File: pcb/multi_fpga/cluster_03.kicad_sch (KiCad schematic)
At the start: 7 parts, among them J15 Cluster3_SpokeBus, J16 Cluster3_Power

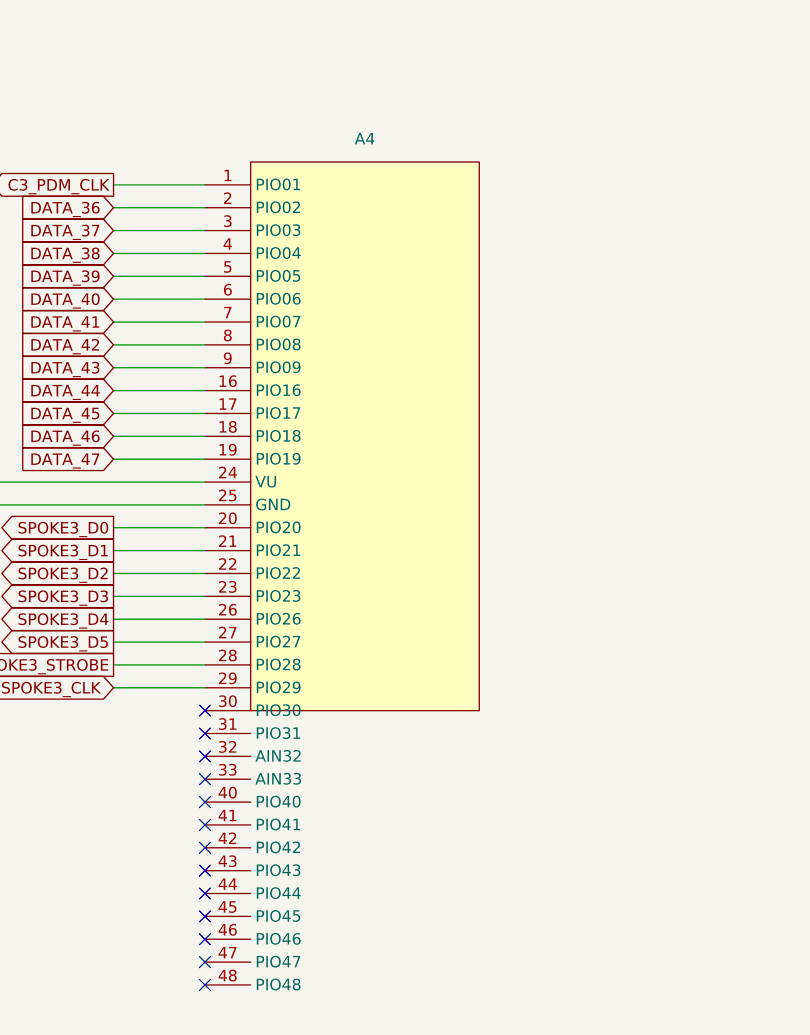
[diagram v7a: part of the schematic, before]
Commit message: Updated FPGA symbols.
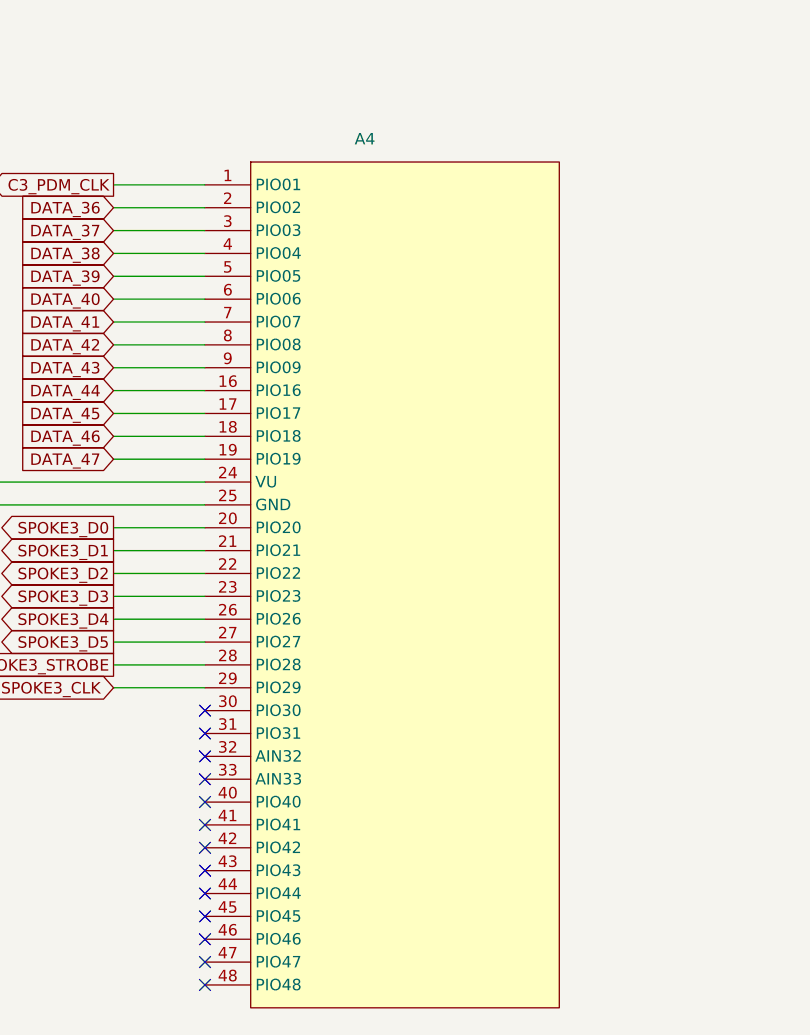
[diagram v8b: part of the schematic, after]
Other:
- moved on the sheet: A4
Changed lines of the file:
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@@
 		(color 0 0 0 0)
 	)
+	(no_connect
+		(at 205.74 196.85)
+	)
+	(no_connect
+		(at 205.74 199.39)
+	)
+	(no_connect
+		(at 205.74 189.23)
+	)
+	(no_connect
+		(at 205.74 204.47)
+	)
+	(no_connect
+		(at 205.74 181.61)
+	)
+	(no_connect
+		(at 205.74 176.53)
+	)
+	(no_connect
+		(at 205.74 186.69)
+	)
+	(no_connect
+		(at 205.74 179.07)
+	)
+	(no_connect
+		(at 205.74 191.77)
+	)
+	(no_connect
+		(at 205.74 173.99)
+	)
+	(no_connect
+		(at 205.74 194.31)
+	)
+	(no_connect
+		(at 205.74 201.93)
+	)
+	(no_connect
+		(at 205.74 184.15)
+	)
 	(wire
 		(pts
@@
 			)
 		)
-		(property "Description" ""
+		(property "Description" "100 nF decoupling capacitor, 0402"
 			(at 327.66 186.69 0)
 			(hide yes)
@@
 			)
 		)
-		(property "Description" ""
+		(property "Description" "Power symbol creates a global label with name \"GND\" , ground"
 			(at 308.61 191.77 0)
 			(hide yes)
@@
 	)
 	(symbol
-		(lib_name "GND_9")
 		(lib_id "power:GND")
 		(at 364.49 113.03 0)
@@
 	)
 	(symbol
-		(lib_name "GND_1")
 		(lib_id "power:GND")
 		(at 160.02 160.02 0)
@@
 			)
 		)
-		(property "Description" ""
+		(property "Description" "Power symbol creates a global label with name \"GND\" , ground"
 			(at 175.26 154.94 0)
 			(hide yes)
@@
 			)
 		)
-		(property "Description" ""
+		(property "Description" "100 nF decoupling capacitor, 0402"
 			(at 289.56 186.69 0)
 			(hide yes)
@@
 			)
 		)
-		(property "Datasheet" ""
+		(property "Datasheet" "http://ww1.microchip.com/downloads/en/DeviceDoc/20001826D.pdf"
 			(at 308.61 181.61 0)
 			(hide yes)
@@
 			)
 		)
-		(property "Description" ""
+		(property "Description" "250mA Low Quiscent Current LDO, 1.8V output, SOT-23"
 			(at 308.61 181.61 0)
 			(hide yes)
@@
 			)
 		)
-		(property "Description" ""
+		(property "Description" "Cluster FPGA module — Pmod JA (8 sig, 200ohm series) + DIP header (13 of 32 GPIO used for local PDM capture); every pin series-resistor protected, no differential-capable I/O (see PHASE4.md Spoke link)"
 			(at 223.52 143.51 0)
 			(hide yes)
@@
 			)
 		)
-		(pin "D1"
+		(pin "1"
+		)
+		(pin "2"
+		)
+		(pin "3"
+		)
+		(pin "4"
+		)
+		(pin "5"
+		)
+		(pin "6"
+		)
+		(pin "7"
+		)
+		(pin "8"
+		)
+		(pin "9"
+		)
+		(pin "16"
+		)
+		(pin "17"
 		)
-		(pin "D2"
+		(pin "18"
 		)
-		(pin "D3"
+		(pin "19"
 		)
-		(pin "D4"
+		(pin "20"
 		)
-		(pin "D5"
+		(pin "21"
 		)
-		(pin "D6"
+		(pin "22"
 		)
-		(pin "D7"
+		(pin "23"
 		)
-		(pin "D8"
+		(pin "24"
 		)
-		(pin "D9"
+		(pin "25"
 		)
-		(pin "D10"
+		(pin "26"
 		)
-		(pin "D11"
+		(pin "27"
 		)
-		(pin "D12"
+		(pin "28"
 		)
-		(pin "D13"
+		(pin "29"
 		)
-		(pin "D24"
+		(pin "30"
 		)
-		(pin "D25"
+		(pin "31"
 		)
-		(pin "D16"
+		(pin "32"
 		)
-		(pin "D17"
+		(pin "33"
 		)
-		(pin "D18"
+		(pin "40"
 		)
-		(pin "D19"
+		(pin "41"
 		)
-		(pin "D20"
+		(pin "42"
 		)
-		(pin "D21"
+		(pin "43"
 		)
-		(pin "D22"
+		(pin "44"
 		)
-		(pin "D23"
+		(pin "45"
+		)
+		(pin "46"
+		)
+		(pin "47"
+		)
+		(pin "48"
 		)
 		(instances
@@
 	)
 	(symbol
-		(lib_name "GND_10")
 		(lib_id "power:GND")
 		(at 318.77 119.38 0)
@@
 			)
 		)
-		(property "Description" ""
+		(property "Description" "Power symbol creates a global label with name \"GND\" , ground"
 			(at 358.14 187.96 0)
 			(hide yes)
@@
 			)
 		)
-		(property "Description" ""
+		(property "Description" "Power symbol creates a global label with name \"+5V\""
 			(at 289.56 173.99 0)
 			(hide yes)
@@
 	)
 	(symbol
-		(lib_name "GND_12")
 		(lib_id "power:GND")
 		(at 285.75 113.03 0)
@@
 			)
 		)
-		(property "Description" ""
+		(property "Description" "Power symbol creates a global label with name \"GND\" , ground"
 			(at 327.66 191.77 0)
 			(hide yes)
@@
 			)
 		)
-		(property "Description" ""
+		(property "Description" "Power symbol creates a global label with name \"+5V\""
 			(at 160.02 144.78 0)
 			(hide yes)
@@
 			)
 		)
-		(property "Description" ""
+		(property "Description" "Power symbol creates a global label with name \"GND\" , ground"
 			(at 289.56 191.77 0)
 			(hide yes)
@@
 	)
 	(symbol
-		(lib_name "GND_11")
 		(lib_id "power:GND")
 		(at 331.47 119.38 0)
@@
 			)
 		)
-		(property "Description" ""
+		(property "Description" "Power symbol creates a global label with name \"+5V\""
 			(at 358.14 177.8 0)
 			(hide yes)
@@
 	)
 	(embedded_fonts no)
-	(no_connect
-		(at 205.74 173.99)
-	)
-	(no_connect
-		(at 205.74 176.53)
-	)
-	(no_connect
-		(at 205.74 179.07)
-	)
-	(no_connect
-		(at 205.74 181.61)
-	)
-	(no_connect
-		(at 205.74 184.15)
-	)
-	(no_connect
-		(at 205.74 186.69)
-	)
-	(no_connect
-		(at 205.74 189.23)
-	)
-	(no_connect
-		(at 205.74 191.77)
-	)
-	(no_connect
-		(at 205.74 194.31)
-	)
-	(no_connect
-		(at 205.74 196.85)
-	)
-	(no_connect
-		(at 205.74 199.39)
-	)
-	(no_connect
-		(at 205.74 201.93)
-	)
-	(no_connect
-		(at 205.74 204.47)
-	)
 )
